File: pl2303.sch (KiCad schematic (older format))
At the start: 23 parts, among them P2 USB_OTG, U2 PL2303, Y1 CRYSTAL

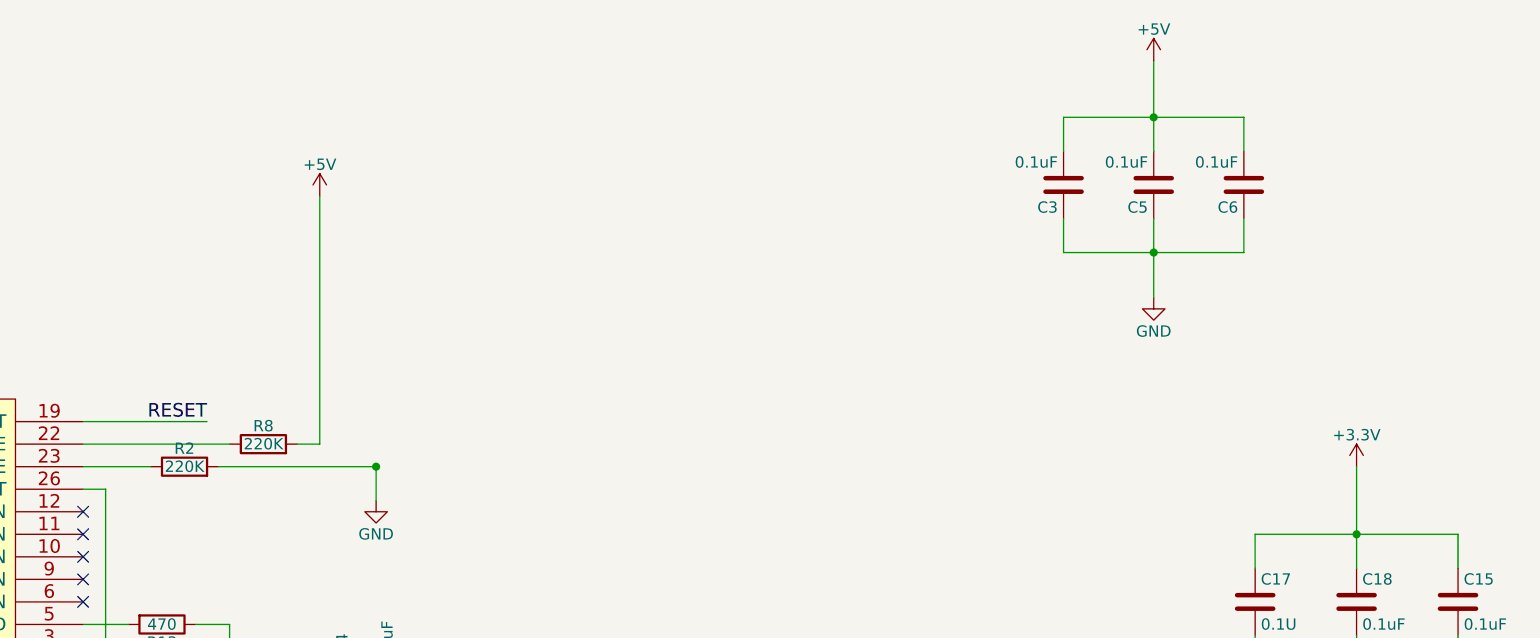
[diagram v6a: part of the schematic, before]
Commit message: Изменения футпринтов и расположения на плате
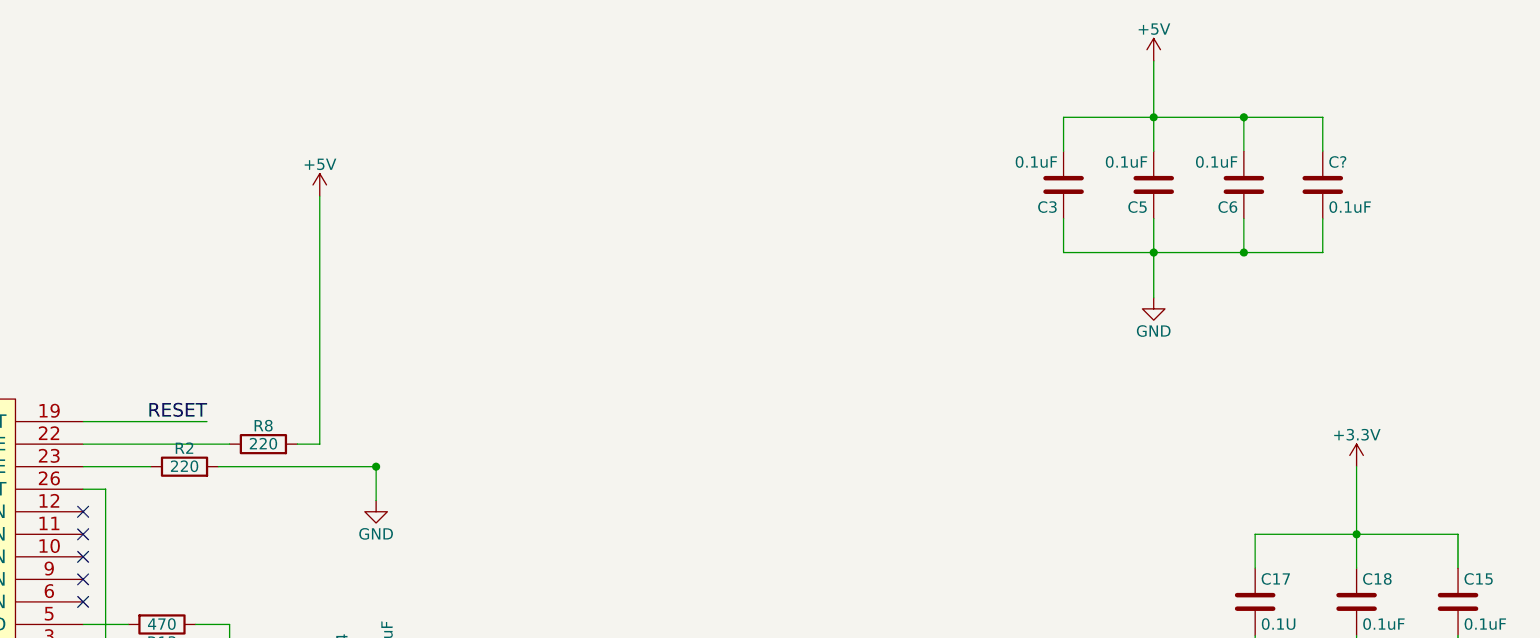
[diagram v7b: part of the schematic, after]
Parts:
- added C?: 0.1uF, symbol C
- C14, C15, C17, C18, C3, C5, C6: footprint Capacitors_SMD:C_0402 -> Capacitors_SMD:C_0805
- D3: footprint LEDs:LED-8MM -> LEDs:LED_0805
- R1, R12, R13, R7: footprint Resistors_SMD:R_0805_HandSoldering -> Resistors_ThroughHole:Resistor_Horizontal_RM10mm
- R2, R8: value 220K -> 220; footprint Resistors_SMD:R_0805_HandSoldering -> Resistors_ThroughHole:Resistor_Horizontal_RM10mm
- R3, R4, R5: footprint Resistors_SMD:R_0402 -> Resistors_SMD:R_0805
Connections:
- net +5V: now also C?.1
- net GND: now also C?.2
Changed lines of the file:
@@
 $Descr A4 11693 8268
 encoding utf-8
-Sheet 4 4
+Sheet 3 4
 Title ""
 Date "20 apr 2016"
@@
 $EndComp
 $Comp
-L GND #PWR024
+L GND #PWR021
 U 1 1 5705278D
 P 9200 4000
-F 0 "#PWR024" H 9200 3750 50  0001 C CNN
+F 0 "#PWR021" H 9200 3750 50  0001 C CNN
 F 1 "GND" H 9200 3850 50  0000 C CNN
 F 2 "" H 9200 4000 50  0000 C CNN
@@
 F 0 "C17" H 8775 3600 50  0000 L CNN
 F 1 "0.1U" H 8775 3400 50  0000 L CNN
-F 2 "Capacitors_SMD:C_0402" H 8788 3350 50  0001 C CNN
+F 2 "Capacitors_SMD:C_0805" H 8788 3350 50  0001 C CNN
 F 3 "" H 8750 3500 50  0000 C CNN
 	1    8750 3500
@@
 F 0 "C18" H 9225 3600 50  0000 L CNN
 F 1 "0.1uF" H 9225 3400 50  0000 L CNN
-F 2 "Capacitors_SMD:C_0402" H 9238 3350 50  0001 C CNN
+F 2 "Capacitors_SMD:C_0805" H 9238 3350 50  0001 C CNN
 F 3 "" H 9200 3500 50  0000 C CNN
 	1    9200 3500
@@
 $EndComp
 $Comp
-L GND #PWR025
+L GND #PWR022
 U 1 1 570529E3
 P 8500 5700
-F 0 "#PWR025" H 8500 5450 50  0001 C CNN
+F 0 "#PWR022" H 8500 5450 50  0001 C CNN
 F 1 "GND" H 8500 5550 50  0000 C CNN
 F 2 "" H 8500 5700 50  0000 C CNN
@@
 F 0 "R3" V 7430 6050 50  0000 C CNN
 F 1 "27" V 7350 6050 50  0000 C CNN
-F 2 "Resistors_SMD:R_0402" V 7280 6050 50  0001 C CNN
+F 2 "Resistors_SMD:R_0805" V 7280 6050 50  0001 C CNN
 F 3 "" H 7350 6050 50  0000 C CNN
 	1    7350 6050
@@
 F 0 "R4" V 7430 6300 50  0000 C CNN
 F 1 "27" V 7350 6300 50  0000 C CNN
-F 2 "Resistors_SMD:R_0402" V 7280 6300 50  0001 C CNN
+F 2 "Resistors_SMD:R_0805" V 7280 6300 50  0001 C CNN
 F 3 "" H 7350 6300 50  0000 C CNN
 	1    7350 6300
@@
 F 0 "R5" V 7780 5850 50  0000 C CNN
 F 1 "1.5K" V 7700 5850 50  0000 C CNN
-F 2 "Resistors_SMD:R_0402" V 7630 5850 50  0001 C CNN
+F 2 "Resistors_SMD:R_0805" V 7630 5850 50  0001 C CNN
 F 3 "" H 7700 5850 50  0000 C CNN
 	1    7700 5850
@@
 F 0 "D3" H 3750 5050 50  0000 C CNN
 F 1 "LED_RX" H 3750 4850 50  0000 C CNN
-F 2 "LEDs:LED-8MM" H 3750 4950 50  0001 C CNN
+F 2 "LEDs:LED_0805" H 3750 4950 50  0001 C CNN
 F 3 "" H 3750 4950 50  0000 C CNN
 	1    3750 4950
@@
 F 0 "R7" V 3180 5200 50  0000 C CNN
 F 1 "220-470" V 3100 5200 50  0000 C CNN
-F 2 "Resistors_SMD:R_0805_HandSoldering" V 3030 5200 50  0001 C CNN
+F 2 "Resistors_ThroughHole:Resistor_Horizontal_RM10mm" V 3030 5200 50  0001 C CNN
 F 3 "" H 3100 5200 50  0000 C CNN
 	1    3100 5200
@@
 $EndComp
 $Comp
-L GND #PWR026
+L GND #PWR023
 U 1 1 570620C0
 P 2950 5500
-F 0 "#PWR026" H 2950 5250 50  0001 C CNN
+F 0 "#PWR023" H 2950 5250 50  0001 C CNN
 F 1 "GND" H 2950 5350 50  0000 C CNN
 F 2 "" H 2950 5500 50  0000 C CNN
@@
 F 0 "C14" H 4825 3900 50  0000 L CNN
 F 1 "0.1uF" H 4825 3700 50  0000 L CNN
-F 2 "Capacitors_SMD:C_0402" H 4838 3650 50  0001 C CNN
+F 2 "Capacitors_SMD:C_0805" H 4838 3650 50  0001 C CNN
 F 3 "" H 4800 3800 50  0000 C CNN
 	1    4800 3800
@@
 $EndComp
 $Comp
-L GND #PWR027
+L GND #PWR024
 U 1 1 570D14D2
 P 950 3800
-F 0 "#PWR027" H 950 3550 50  0001 C CNN
+F 0 "#PWR024" H 950 3550 50  0001 C CNN
 F 1 "GND" H 950 3650 50  0000 C CNN
 F 2 "" H 950 3800 50  0000 C CNN
@@
 F 0 "R1" V 2880 5200 50  0000 C CNN
 F 1 "220-470" V 2800 5200 50  0000 C CNN
-F 2 "Resistors_SMD:R_0805_HandSoldering" V 2730 5200 50  0001 C CNN
+F 2 "Resistors_ThroughHole:Resistor_Horizontal_RM10mm" V 2730 5200 50  0001 C CNN
 F 3 "" H 2800 5200 50  0000 C CNN
 	1    2800 5200
@@
 NoConn ~ 3550 3700
 $Comp
-L GND #PWR028
+L GND #PWR025
 U 1 1 570D2EBB
 P 2450 5100
-F 0 "#PWR028" H 2450 4850 50  0001 C CNN
+F 0 "#PWR025" H 2450 4850 50  0001 C CNN
 F 1 "GND" H 2450 4950 50  0000 C CNN
 F 2 "" H 2450 5100 50  0000 C CNN
@@
 P 4000 2900
 F 0 "R2" V 4080 2900 50  0000 C CNN
-F 1 "220K" V 4000 2900 50  0000 C CNN
-F 2 "Resistors_SMD:R_0805_HandSoldering" V 3930 2900 50  0001 C CNN
+F 1 "220" V 4000 2900 50  0000 C CNN
+F 2 "Resistors_ThroughHole:Resistor_Horizontal_RM10mm" V 3930 2900 50  0001 C CNN
 F 3 "" H 4000 2900 50  0000 C CNN
 	1    4000 2900
@@
 $EndComp
 $Comp
-L GND #PWR029
+L GND #PWR026
 U 1 1 570D2F71
 P 4850 3050
-F 0 "#PWR029" H 4850 2800 50  0001 C CNN
+F 0 "#PWR026" H 4850 2800 50  0001 C CNN
 F 1 "GND" H 4850 2900 50  0000 C CNN
 F 2 "" H 4850 3050 50  0000 C CNN
@@
 P 4350 2800
 F 0 "R8" V 4430 2800 50  0000 C CNN
-F 1 "220K" V 4350 2800 50  0000 C CNN
-F 2 "Resistors_SMD:R_0805_HandSoldering" V 4280 2800 50  0001 C CNN
+F 1 "220" V 4350 2800 50  0000 C CNN
+F 2 "Resistors_ThroughHole:Resistor_Horizontal_RM10mm" V 4280 2800 50  0001 C CNN
 F 3 "" H 4350 2800 50  0000 C CNN
 	1    4350 2800
@@
 $EndComp
 $Comp
-L +3.3V #PWR030
+L +3.3V #PWR027
 U 1 1 570D3933
 P 9200 2900
-F 0 "#PWR030" H 9200 2750 50  0001 C CNN
+F 0 "#PWR027" H 9200 2750 50  0001 C CNN
 F 1 "+3.3V" H 9200 3040 50  0000 C CNN
 F 2 "" H 9200 2900 50  0000 C CNN
@@
 F 0 "C3" H 7925 1750 50  0000 L CNN
 F 1 "0.1uF" H 7925 1550 50  0000 L CNN
-F 2 "Capacitors_SMD:C_0402" H 7938 1500 50  0001 C CNN
+F 2 "Capacitors_SMD:C_0805" H 7938 1500 50  0001 C CNN
 F 3 "" H 7900 1650 50  0000 C CNN
 	1    7900 1650
@@
 F 0 "C5" H 8325 1750 50  0000 L CNN
 F 1 "0.1uF" H 8325 1550 50  0000 L CNN
-F 2 "Capacitors_SMD:C_0402" H 8338 1500 50  0001 C CNN
+F 2 "Capacitors_SMD:C_0805" H 8338 1500 50  0001 C CNN
 F 3 "" H 8300 1650 50  0000 C CNN
 	1    8300 1650
@@
 F 0 "C6" H 8725 1750 50  0000 L CNN
 F 1 "0.1uF" H 8725 1550 50  0000 L CNN
-F 2 "Capacitors_SMD:C_0402" H 8738 1500 50  0001 C CNN
+F 2 "Capacitors_SMD:C_0805" H 8738 1500 50  0001 C CNN
 F 3 "" H 8700 1650 50  0000 C CNN
 	1    8700 1650
@@
 $EndComp
 $Comp
-L +5V #PWR031
+L +5V #PWR028
 U 1 1 5717E4F4
 P 8300 1100
-F 0 "#PWR031" H 8300 950 50  0001 C CNN
+F 0 "#PWR028" H 8300 950 50  0001 C CNN
 F 1 "+5V" H 8300 1240 50  0000 C CNN
 F 2 "" H 8300 1100 50  0000 C CNN
@@
 $EndComp
 $Comp
-L GND #PWR032
+L GND #PWR029
 U 1 1 5717E503
 P 8300 2150
-F 0 "#PWR032" H 8300 1900 50  0001 C CNN
+F 0 "#PWR029" H 8300 1900 50  0001 C CNN
 F 1 "GND" H 8300 2000 50  0000 C CNN
 F 2 "" H 8300 2150 50  0000 C CNN
@@
 $EndComp
 $Comp
-L +5V #PWR033
+L +5V #PWR030
 U 1 1 5717F490
 P 2450 1450
-F 0 "#PWR033" H 2450 1300 50  0001 C CNN
+F 0 "#PWR030" H 2450 1300 50  0001 C CNN
 F 1 "+5V" H 2450 1590 50  0000 C CNN
 F 2 "" H 2450 1450 50  0000 C CNN
@@
 F 0 "R13" V 3980 3600 50  0000 C CNN
 F 1 "470" V 3900 3600 50  0000 C CNN
-F 2 "Resistors_SMD:R_0805_HandSoldering" V 3830 3600 50  0001 C CNN
+F 2 "Resistors_ThroughHole:Resistor_Horizontal_RM10mm" V 3830 3600 50  0001 C CNN
 F 3 "" H 3900 3600 50  0000 C CNN
 	1    3900 3600
@@
 F 0 "R12" V 3880 3900 50  0000 C CNN
 F 1 "470" V 3800 3900 50  0000 C CNN
-F 2 "Resistors_SMD:R_0805_HandSoldering" V 3730 3900 50  0001 C CNN
+F 2 "Resistors_ThroughHole:Resistor_Horizontal_RM10mm" V 3730 3900 50  0001 C CNN
 F 3 "" H 3800 3900 50  0000 C CNN
 	1    3800 3900
@@
 	7900 1800 7900 1950
 Wire Wire Line
-	7900 1950 8700 1950
+	7900 1950 9050 1950
 Wire Wire Line
 	8700 1950 8700 1800
@@
 	7900 1350 7900 1500
 Wire Wire Line
-	7900 1350 8700 1350
+	7900 1350 9050 1350
 Wire Wire Line
 	8300 1100 8300 1500
@@
 	2750 1450 2750 2300
 $Comp
-L +3.3V #PWR034
+L +3.3V #PWR031
 U 1 1 571E53D2
 P 2750 1450
-F 0 "#PWR034" H 2750 1300 50  0001 C CNN
+F 0 "#PWR031" H 2750 1300 50  0001 C CNN
 F 1 "+3.3V" H 2750 1590 50  0000 C CNN
 F 2 "" H 2750 1450 50  0000 C CNN
@@
 $EndComp
 $Comp
-L +3.3V #PWR035
+L +3.3V #PWR032
 U 1 1 571E5683
 P 7700 5350
-F 0 "#PWR035" H 7700 5200 50  0001 C CNN
+F 0 "#PWR032" H 7700 5200 50  0001 C CNN
 F 1 "+3.3V" H 7700 5490 50  0000 C CNN
 F 2 "" H 7700 5350 50  0000 C CNN
@@
 F 0 "C15" H 9675 3600 50  0000 L CNN
 F 1 "0.1uF" H 9675 3400 50  0000 L CNN
-F 2 "Capacitors_SMD:C_0402" H 9688 3350 50  0001 C CNN
+F 2 "Capacitors_SMD:C_0805" H 9688 3350 50  0001 C CNN
 F 3 "" H 9650 3500 50  0000 C CNN
 	1    9650 3500
@@
 	8500 5000 8500 4400
 $Comp
-L +5V #PWR036
+L +5V #PWR033
 U 1 1 571E81DD
 P 8500 4400
-F 0 "#PWR036" H 8500 4250 50  0001 C CNN
+F 0 "#PWR033" H 8500 4250 50  0001 C CNN
 F 1 "+5V" H 8500 4540 50  0000 C CNN
 F 2 "" H 8500 4400 50  0000 C CNN
@@
 $EndComp
 $Comp
-L +5V #PWR037
+L +5V #PWR034
 U 1 1 571E851C
 P 4600 1700
-F 0 "#PWR037" H 4600 1550 50  0001 C CNN
+F 0 "#PWR034" H 4600 1550 50  0001 C CNN
 F 1 "+5V" H 4600 1840 50  0000 C CNN
 F 2 "" H 4600 1700 50  0000 C CNN
@@
 	8500 5400 8650 5400
 NoConn ~ 8650 5300
+$Comp
+L C C?
+U 1 1 5739D45A
+P 9050 1650
+F 0 "C?" H 9075 1750 50  0000 L CNN
+F 1 "0.1uF" H 9075 1550 50  0000 L CNN
+F 2 "" H 9088 1500 50  0000 C CNN
+F 3 "" H 9050 1650 50  0000 C CNN
+	1    9050 1650
+	1    0    0    -1
+$EndComp
+Wire Wire Line
+	9050 1350 9050 1500
+Connection ~ 8700 1350
+Wire Wire Line
+	9050 1950 9050 1800
+Connection ~ 8700 1950
 $EndSCHEMATC

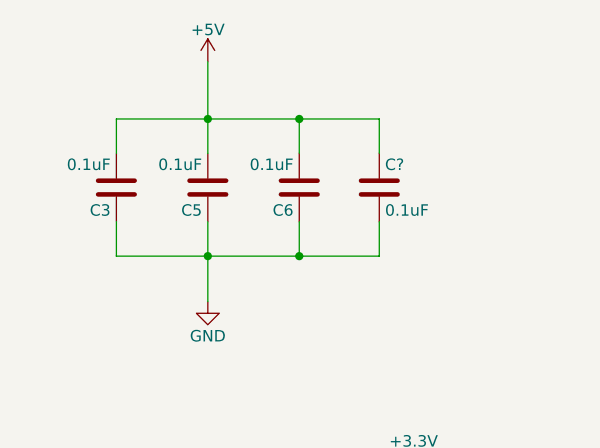
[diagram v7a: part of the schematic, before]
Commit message: разводка питания
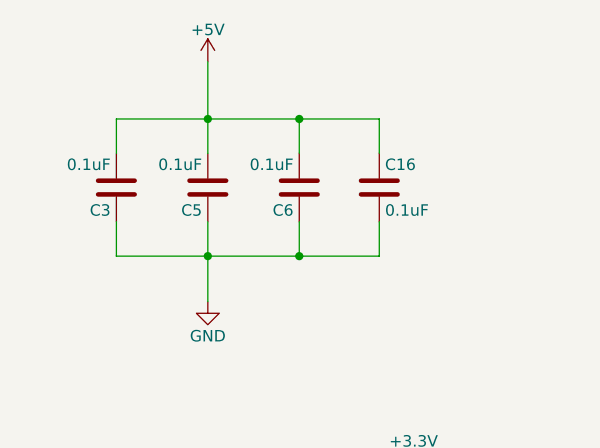
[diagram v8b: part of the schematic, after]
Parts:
- C16: renamed from C?; footprint (none) -> Capacitors_SMD:C_0805
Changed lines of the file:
@@
 NoConn ~ 8650 5300
 $Comp
-L C C?
+L C C16
 U 1 1 5739D45A
 P 9050 1650
-F 0 "C?" H 9075 1750 50  0000 L CNN
+F 0 "C16" H 9075 1750 50  0000 L CNN
 F 1 "0.1uF" H 9075 1550 50  0000 L CNN
-F 2 "" H 9088 1500 50  0000 C CNN
+F 2 "Capacitors_SMD:C_0805" H 9088 1500 50  0001 C CNN
 F 3 "" H 9050 1650 50  0000 C CNN
 	1    9050 1650
